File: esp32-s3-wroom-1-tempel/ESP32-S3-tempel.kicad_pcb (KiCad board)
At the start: 2 copper layers, 68.4 x 51.3 mm, 33 parts, among them J1 USB, J2 USB2UART, J3 West, J4 East, J5 Nort, J6 South, Q1 SS8050, Q2 SS8050, SW1 RST, SW2 Boot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

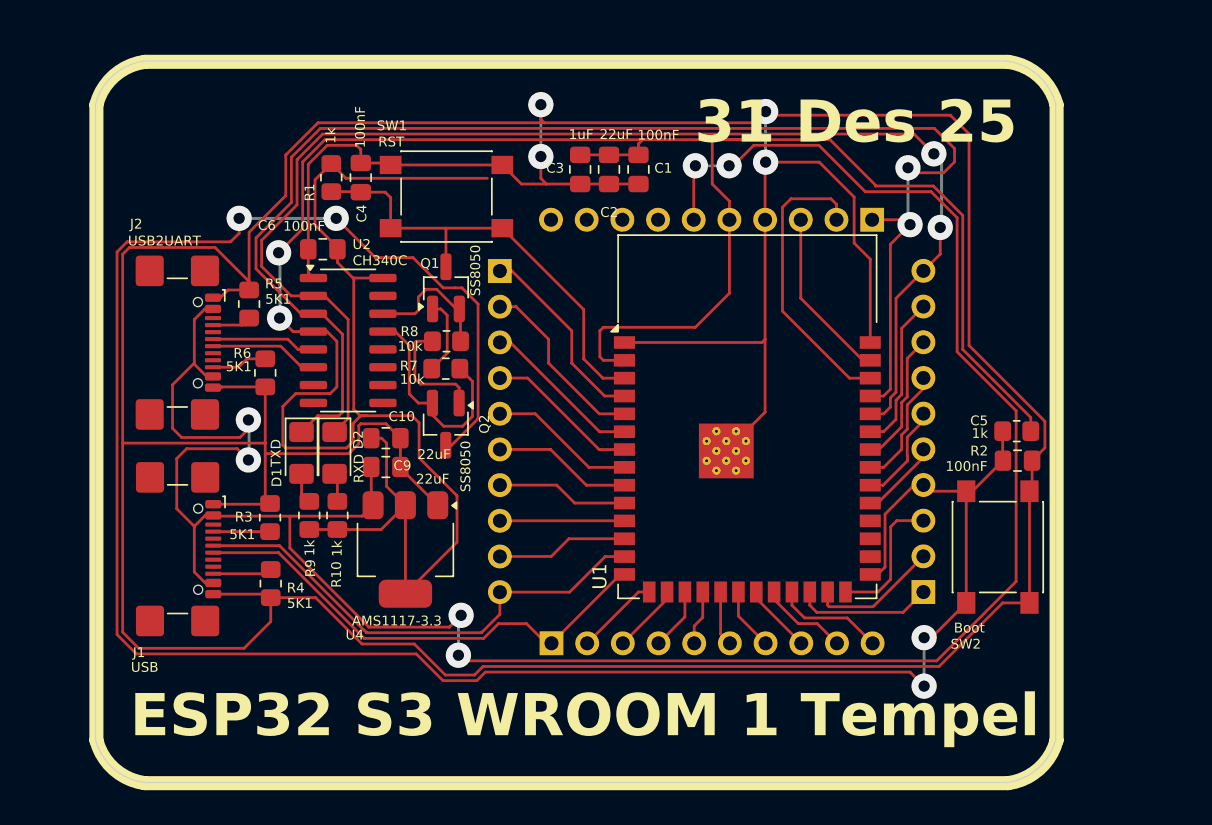
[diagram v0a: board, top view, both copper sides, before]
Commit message: feat: make esp32-s3-wroom-1 temple route more ticker
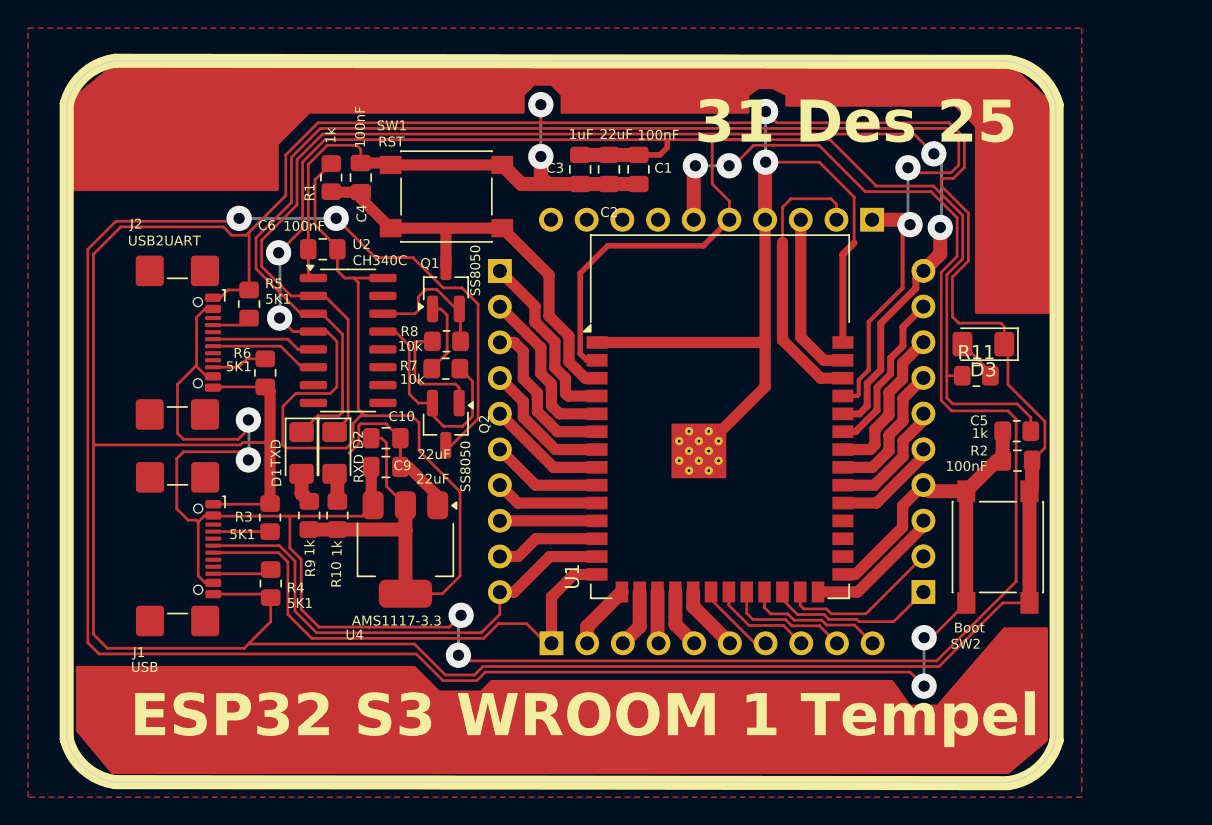
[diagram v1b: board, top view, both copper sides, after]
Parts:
- added D3: TXD, LED_SMD:LED_1206_3216Metric_Pad1.42x1.75mm_HandSolder, F.Cu at (187.2, 101.2)
- added R11: 1k, Resistor_SMD:R_0805_2012Metric_Pad1.20x1.40mm_HandSolder, F.Cu at (186.8, 103.5)
- U1: value ESP32-S3-WROOM-1U -> ESP32-S3-WROOM-1
- moved U1 1.95 mm to (168.5, 106.4)
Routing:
- net GND: track 353.0 -> 371.3 mm
- net /IO0: track 161.4 -> 179.2 mm
- net +5V: track 168.6 -> 176.0 mm
- net /EN: track 32.8 -> 38.5 mm
- net +3.3V: track 208.6 -> 212.9 mm
- net Net-(D3-A): track 0.00 -> 3.07 mm
- net /IO14: track 6.30 -> 8.82 mm
- net /IO48: track 9.29 -> 11.7 mm
- net /IO47: track 9.84 -> 12.1 mm
- net /IO13: track 4.98 -> 7.22 mm
- net Net-(D1-A): track 2.19 -> 4.38 mm
- net /USB_D+: track 34.5 -> 36.6 mm
- net /IO21: track 7.81 -> 9.86 mm
- net Net-(D2-A): track 2.05 -> 4.09 mm
- net /IO8: track 9.39 -> 7.44 mm
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- added copper zone on F.Cu, net +3.3V
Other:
- board size 68.4 x 51.3 mm -> 70.4 x 51.4 mm
